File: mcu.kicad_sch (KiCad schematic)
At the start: 10 parts, among them J11 USB_C_Receptacle_USB2.0_16P, U4 ESP32-S3-WROOM-1, U5 STM32C011F4Ux

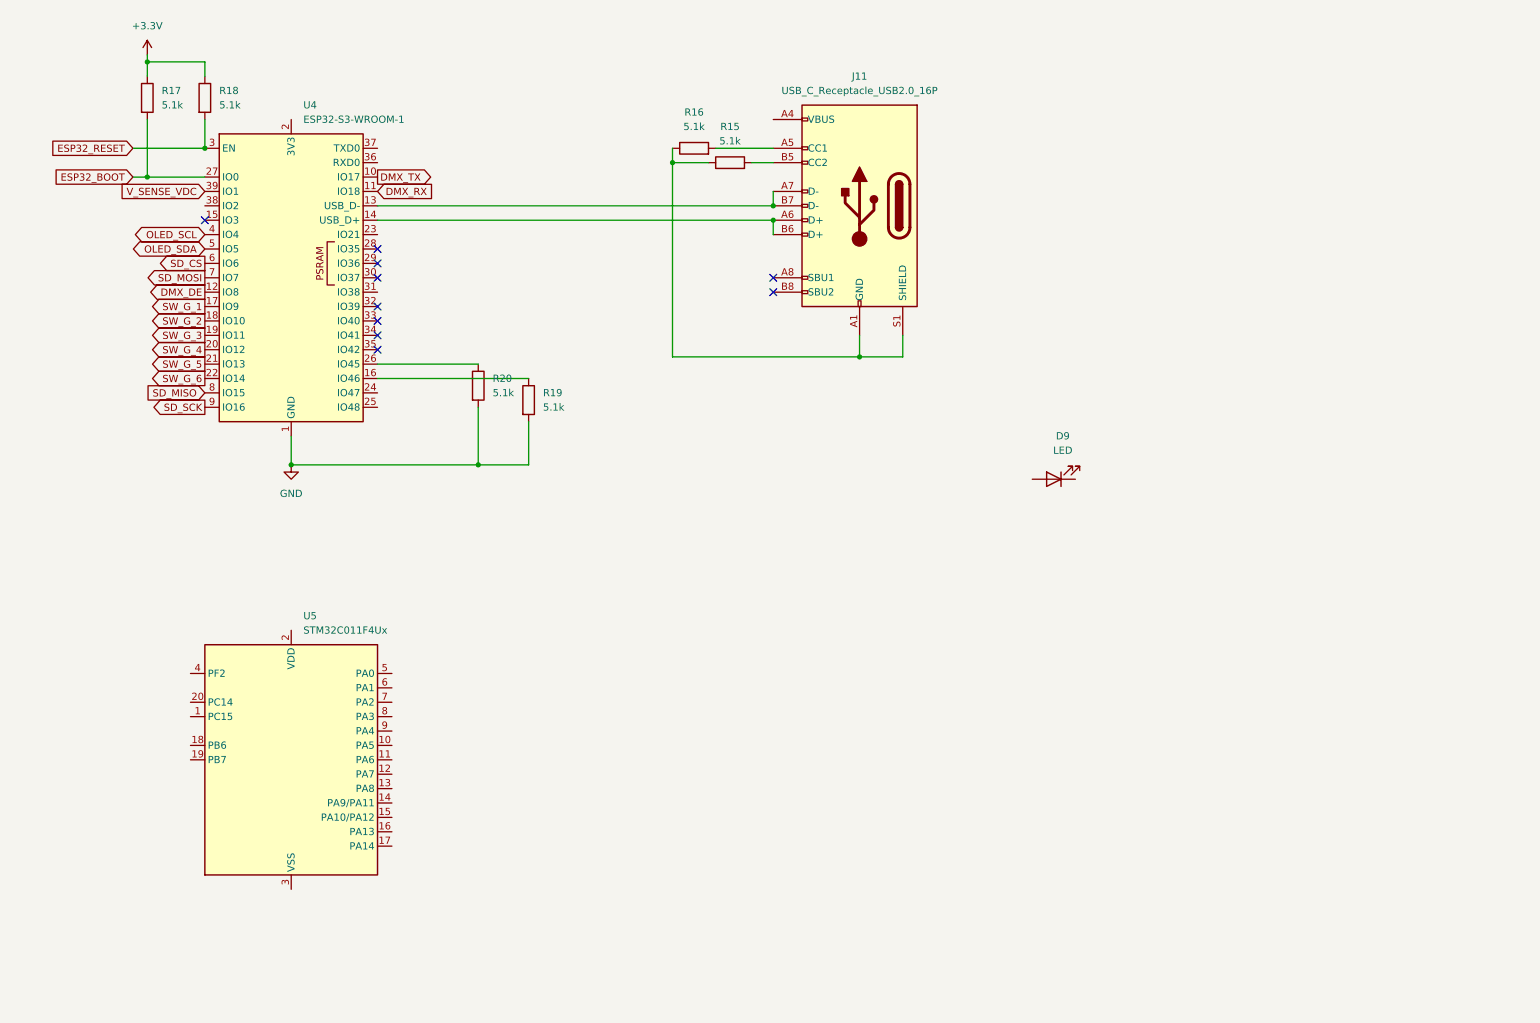
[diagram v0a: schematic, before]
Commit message: mcu pinouts and extras
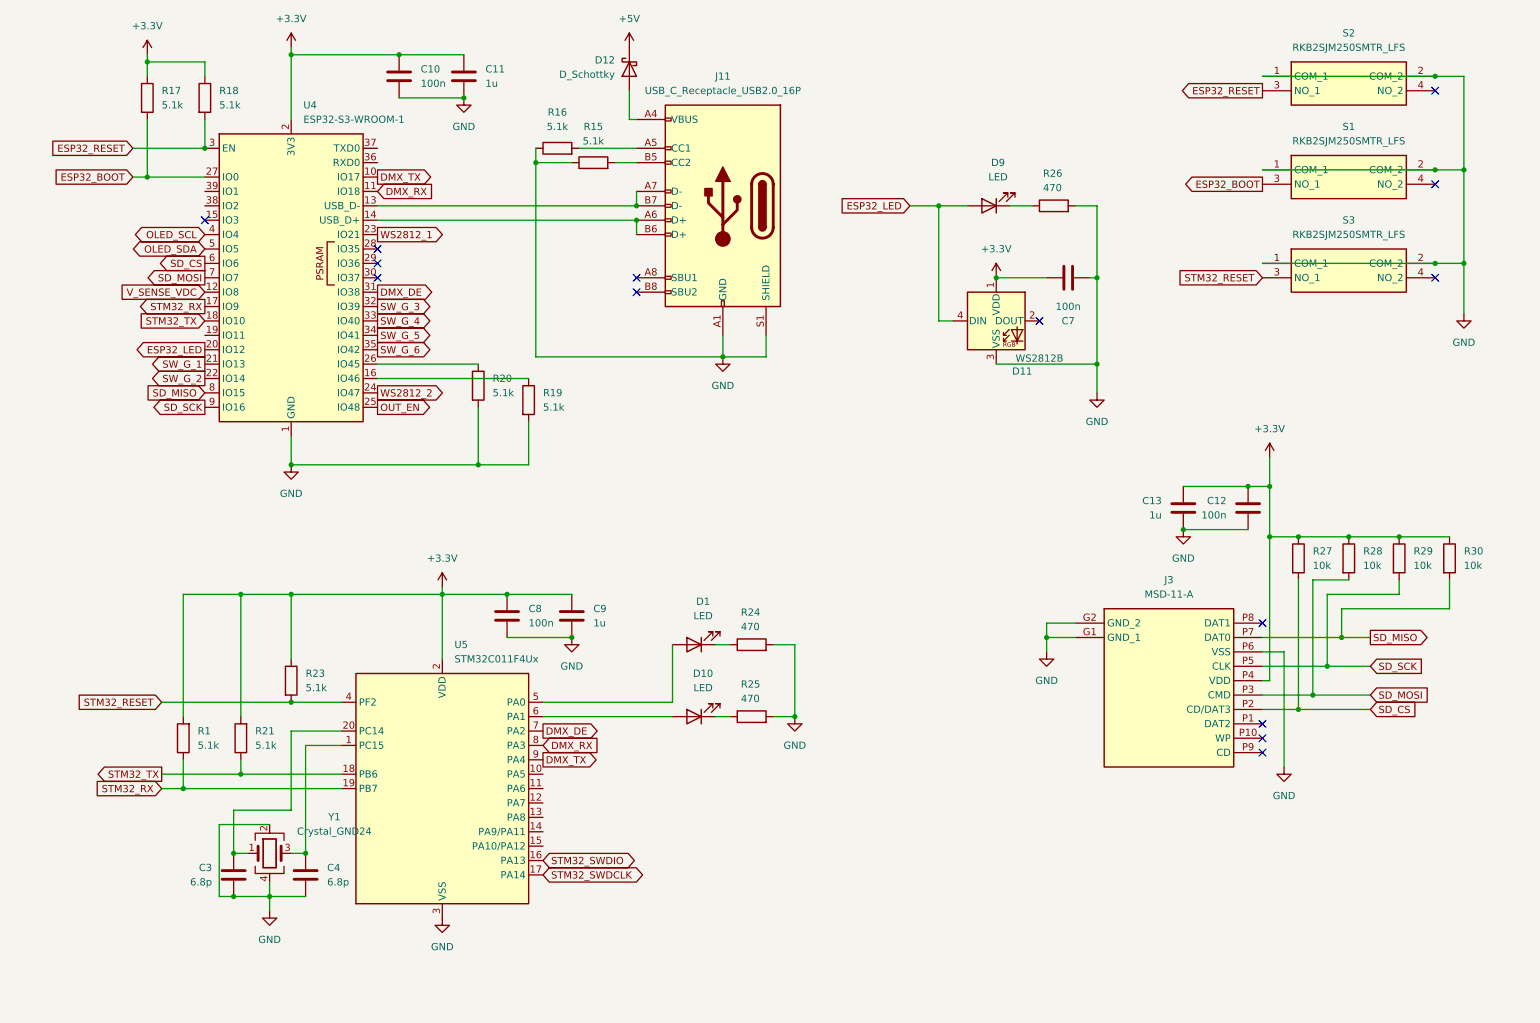
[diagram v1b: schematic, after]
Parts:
- added C10, C12, C7, C8: 100n, Capacitor_SMD:C_0603_1608Metric_Pad1.08x0.95mm_HandSolder, symbol Device:C
- added C11, C13, C9: 1u, Capacitor_SMD:C_0603_1608Metric_Pad1.08x0.95mm_HandSolder, symbol Device:C
- added C3, C4: 6.8p, Capacitor_SMD:C_0603_1608Metric_Pad1.08x0.95mm_HandSolder, symbol Device:C
- added D1, D10: LED, LED_SMD:LED_0603_1608Metric_Pad1.05x0.95mm_HandSolder, symbol Device:LED
- added D11: WS2812B, LED_SMD:LED_WS2812B_PLCC4_5.0x5.0mm_P3.2mm, symbol LED:WS2812B
- added D12: D_Schottky, Diode_SMD:D_SOD-323_HandSoldering, symbol Device:D_Schottky
- added J3: MSD-11-A, SamacSys_Parts:MSD11A, symbol SamacSys_Parts:MSD-11-A
- added R1, R21, R23: 5.1k, Resistor_SMD:R_0603_1608Metric_Pad0.98x0.95mm_HandSolder, symbol Device:R
- added R24, R25, R26: 470, Resistor_SMD:R_0603_1608Metric_Pad0.98x0.95mm_HandSolder, symbol Device:R
- added R27, R28, R29, R30: 10k, Resistor_SMD:R_0603_1608Metric_Pad0.98x0.95mm_HandSolder, symbol Device:R
- added S1, S2, S3: RKB2SJM250SMTR_LFS, SamacSys_Parts:RKB2SJM250SMTRLFS, symbol SamacSys_Parts:RKB2SJM250SMTR_LFS
- added Y1: Crystal_GND24, Crystal:Crystal_SMD_Abracon_ABM8AIG-4Pin_3.2x2.5mm, symbol Device:Crystal_GND24
- R17, R18, R19, R20: footprint (none) -> Resistor_SMD:R_0603_1608Metric_Pad0.98x0.95mm_HandSolder
- U4: footprint RF_Module:ESP32-S2-MINI-1 -> RF_Module:ESP32-S3-WROOM-2
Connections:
- net +3.3V: now also U4.2 (3V3), U5.2 (VDD), C10.1, C11.1, C12.1, C13.1, C7.1, C8.1, C9.1, D11.1 (VDD), J3.P4 (VDD), R1.2, R21.2, R23.1, R27.1, R28.1, R29.1, R30.1
- net DMX_DE: now also U4.31 (IO38), U5.7 (PA2); no longer U4.12 (IO8)
- net DMX_RX: now also U5.8 (PA3)
- net DMX_TX: now also U5.9 (PA4)
- net ESP32_BOOT: now also S1.3 (NO_1)
- net ESP32_RESET: now also S2.3 (NO_1)
- net GND: now also J11.A1 (GND), J11.A12 (GND), J11.B1 (GND), J11.B12 (GND), J11.S1 (SHIELD), R15.1, R16.1, U5.3 (VSS), C10.2, C11.2, C12.2, C13.2, C3.2, C4.2, C7.2, C8.2, C9.2, D11.3 (VSS), J3.G1 (GND_1), J3.G2 (GND_2), J3.P6 (VSS), R24.2, R25.2, R26.2, S1.1 (COM_1), S1.2 (COM_2), S2.1 (COM_1), S2.2 (COM_2), S3.1 (COM_1), S3.2 (COM_2), Y1.2, Y1.4
- net SD_CS: now also J3.P2 (CD/DAT3), R27.2
- net SD_MISO: now also J3.P7 (DAT0), R30.2
- net SD_MOSI: now also J3.P3 (CMD), R28.2
- net SD_SCK: now also J3.P5 (CLK), R29.2
- net SW_G_1: now also U4.21 (IO13); no longer U4.17 (IO9)
- net SW_G_2: now also U4.22 (IO14); no longer U4.18 (IO10)
- net SW_G_3: now also U4.32 (IO39); no longer U4.19 (IO11)
- net SW_G_4: now also U4.33 (IO40); no longer U4.20 (IO12)
- net SW_G_5: now also U4.34 (IO41); no longer U4.21 (IO13)
- net SW_G_6: now also U4.35 (IO42); no longer U4.22 (IO14)
- net V_SENSE_VDC: now also U4.12 (IO8); no longer U4.39 (IO1)
- net WS2812_1: now reaches U4.23 (IO21)
- net WS2812_2: now reaches U4.24 (IO47)
- net OUT_EN: now reaches U4.25 (IO48)
- net at D9.1 (K): now also R26.1
- net ESP32_LED: now reaches D9.2 (A)
- net ESP32_LED: now also U4.20 (IO12), D11.4 (DIN)
- net at U5.1 (PC15): now also C4.1, Y1.3
- net STM32_SWDIO: now reaches U5.16 (PA13)
- net STM32_SWDCLK: now reaches U5.17 (PA14)
- net STM32_TX: now reaches U5.18 (PB6)
- net STM32_TX: now also U4.18 (IO10), R21.1
- net STM32_RX: now reaches U5.19 (PB7)
- net STM32_RX: now also U4.17 (IO9), R1.1
- net at U5.20 (PC14): now also C3.1, Y1.1
- net STM32_RESET: now reaches U5.4 (PF2)
- net STM32_RESET: now also R23.2, S3.3 (NO_1)
- net at U5.5 (PA0): now also D1.2 (A)
- net at U5.6 (PA1): now also D10.2 (A)
- net at J11.A4 (VBUS), J11.A9 (VBUS), J11.B4 (VBUS)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: now also D12.2 (A)
- new net: D1.1 (K), R24.1
- new net: D10.1 (K), R25.1
- new net +5V: D12.1 (K)
- no-connect marks 10 -> 14
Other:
- moved on the sheet: D9, J11, R15, R16, U5

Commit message: power circuitry
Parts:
- removed D12: D_Schottky, Diode_SMD:D_SOD-323_HandSoldering, symbol Device:D_Schottky
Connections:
- net VBUS: now reaches J11.A4 (VBUS), J11.A9 (VBUS), J11.B4 (VBUS), J11.B9 (VBUS)
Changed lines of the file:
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@@
 	(wire
 		(pts
-			(xy 125.73 33.02) (xy 125.73 38.1)
+			(xy 125.73 30.48) (xy 125.73 38.1)
 		)
 		(stroke
@@
 	)
 	(global_label "STM32_RESET"
-		(shape input)
+		(shape output)
 		(at 237.49 66.04 180)
 		(fields_autoplaced yes)
@@
 	)
 	(symbol
-		(lib_id "Device:D_Schottky")
-		(at 125.73 29.21 90)
-		(mirror x)
-		(unit 1)
-		(exclude_from_sim no)
-		(in_bom yes)
-		(on_board yes)
-		(dnp no)
-		(property "Reference" "D12"
-			(at 123.19 27.6224 90)
-			(effects
-				(font
-					(size 1.27 1.27)
-				)
-				(justify left)
-			)
-		)
-		(property "Value" "D_Schottky"
-			(at 123.19 30.1624 90)
-			(effects
-				(font
-					(size 1.27 1.27)
-				)
-				(justify left)
-			)
-		)
-		(property "Footprint" "Diode_SMD:D_SOD-323_HandSoldering"
-			(at 125.73 29.21 0)
-			(effects
-				(font
-					(size 1.27 1.27)
-				)
-				(hide yes)
-			)
-		)
-		(property "Datasheet" "~"
-			(at 125.73 29.21 0)
-			(effects
-				(font
-					(size 1.27 1.27)
-				)
-				(hide yes)
-			)
-		)
-		(property "Description" "Schottky diode"
-			(at 125.73 29.21 0)
-			(effects
-				(font
-					(size 1.27 1.27)
-				)
-				(hide yes)
-			)
-		)
-		(pin "1"
-		)
-		(pin "2"
-		)
-		(instances
-			(project ""
-				(path "/bd7590c0-6a37-4bf0-a9f2-f26180744ceb/57a6da49-ac9c-48a2-9772-b91851c32cdb"
-					(reference "D12")
-					(unit 1)
-				)
-			)
-		)
-	)
-	(symbol
 		(lib_id "power:GND")
 		(at 96.52 34.29 0)
@@
 	)
 	(symbol
-		(lib_id "power:+5V")
-		(at 125.73 25.4 0)
-		(unit 1)
-		(exclude_from_sim no)
-		(in_bom yes)
-		(on_board yes)
-		(dnp no)
-		(fields_autoplaced yes)
-		(property "Reference" "#PWR025"
-			(at 125.73 29.21 0)
-			(effects
-				(font
-					(size 1.27 1.27)
-				)
-				(hide yes)
-			)
-		)
-		(property "Value" "+5V"
-			(at 125.73 20.32 0)
-			(effects
-				(font
-					(size 1.27 1.27)
-				)
-			)
-		)
-		(property "Footprint" ""
-			(at 125.73 25.4 0)
-			(effects
-				(font
-					(size 1.27 1.27)
-				)
-				(hide yes)
-			)
-		)
-		(property "Datasheet" ""
-			(at 125.73 25.4 0)
-			(effects
-				(font
-					(size 1.27 1.27)
-				)
-				(hide yes)
-			)
-		)
-		(property "Description" "Power symbol creates a global label with name \"+5V\""
-			(at 125.73 25.4 0)
-			(effects
-				(font
-					(size 1.27 1.27)
-				)
-				(hide yes)
-			)
-		)
-		(pin "1"
-		)
-		(instances
-			(project ""
-				(path "/bd7590c0-6a37-4bf0-a9f2-f26180744ceb/57a6da49-ac9c-48a2-9772-b91851c32cdb"
-					(reference "#PWR025")
-					(unit 1)
-				)
-			)
-		)
-	)
-	(symbol
 		(lib_id "Device:C")
 		(at 68.58 171.45 0)
@@
 					(unit 1)
 				)
+			)
+		)
+	)
+	(symbol
+		(lib_id "power:VBUS")
+		(at 125.73 30.48 0)
+		(unit 1)
+		(exclude_from_sim no)
+		(in_bom yes)
+		(on_board yes)
+		(dnp no)
+		(fields_autoplaced yes)
+		(property "Reference" "#PWR025"
+			(at 125.73 34.29 0)
+			(effects
+				(font
+					(size 1.27 1.27)
+				)
+				(hide yes)
+			)
+		)
+		(property "Value" "VBUS"
+			(at 125.73 25.4 0)
+			(effects
+				(font
+					(size 1.27 1.27)
+				)
+			)
+		)
+		(property "Footprint" ""
+			(at 125.73 30.48 0)
+			(effects
+				(font
+					(size 1.27 1.27)
+				)
+				(hide yes)
+			)
+		)
+		(property "Datasheet" ""
+			(at 125.73 30.48 0)
+			(effects
+				(font
+					(size 1.27 1.27)
+				)
+				(hide yes)
+			)
+		)
+		(property "Description" "Power symbol creates a global label with name \"VBUS\""
+			(at 125.73 30.48 0)
+			(effects
+				(font
+					(size 1.27 1.27)
+				)
+				(hide yes)
+			)
+		)
+		(pin "1"
+		)
+		(instances
+			(project ""
+				(path "/bd7590c0-6a37-4bf0-a9f2-f26180744ceb/57a6da49-ac9c-48a2-9772-b91851c32cdb"
+					(reference "#PWR025")
+					(unit 1)
+				)

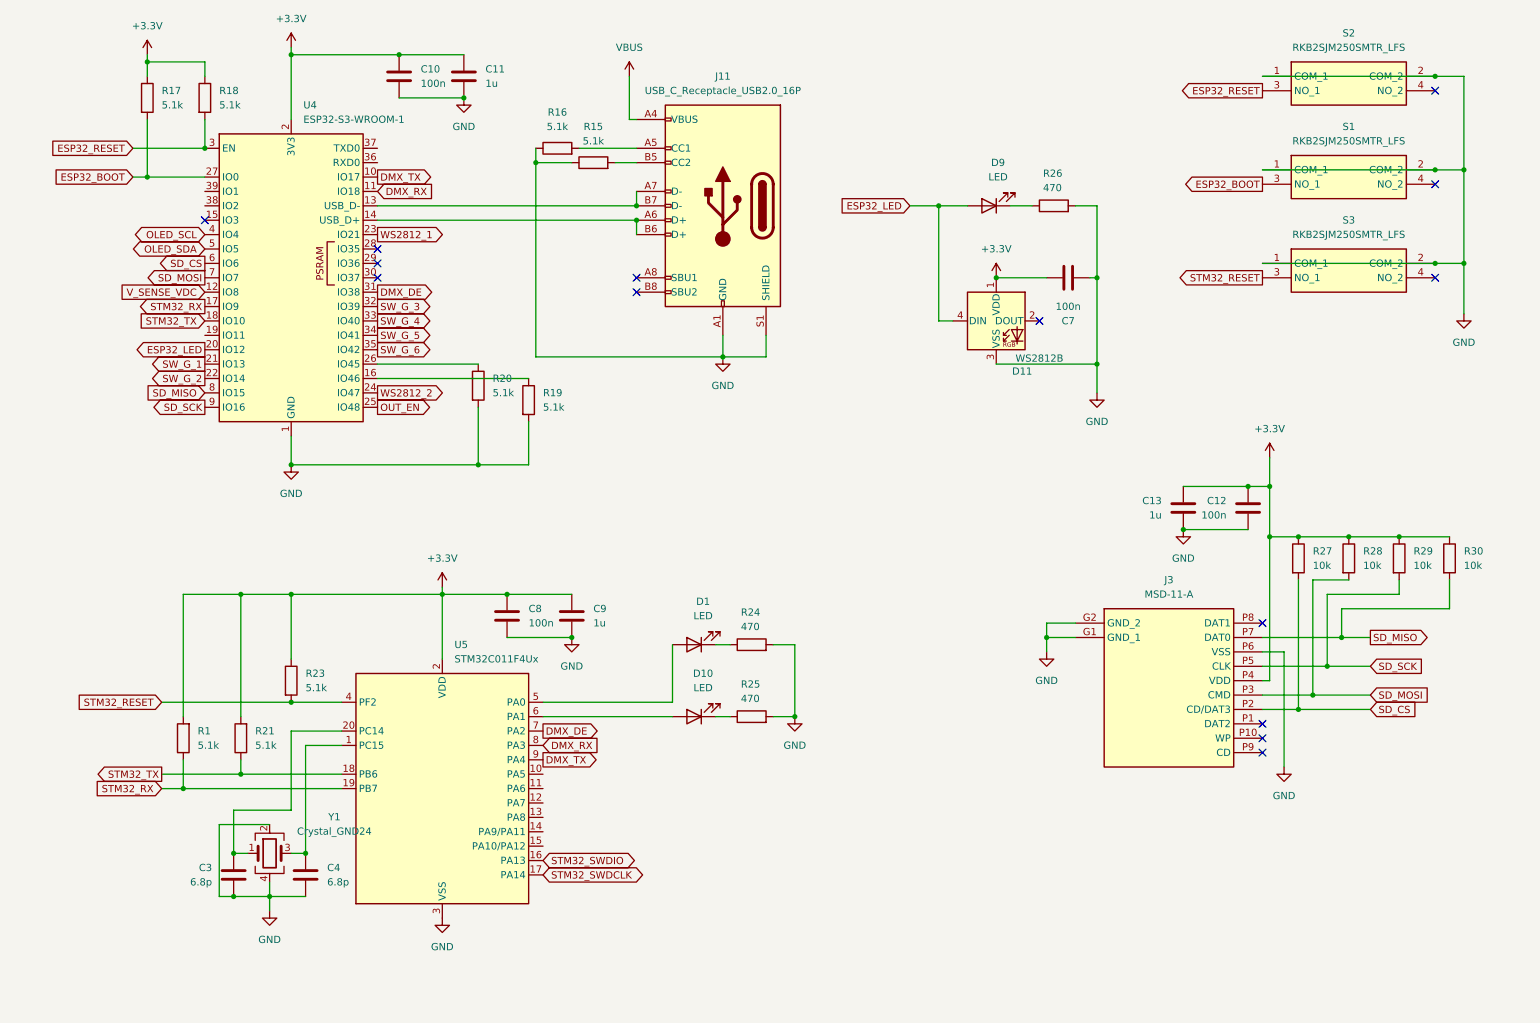
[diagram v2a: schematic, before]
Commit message: add probe headers
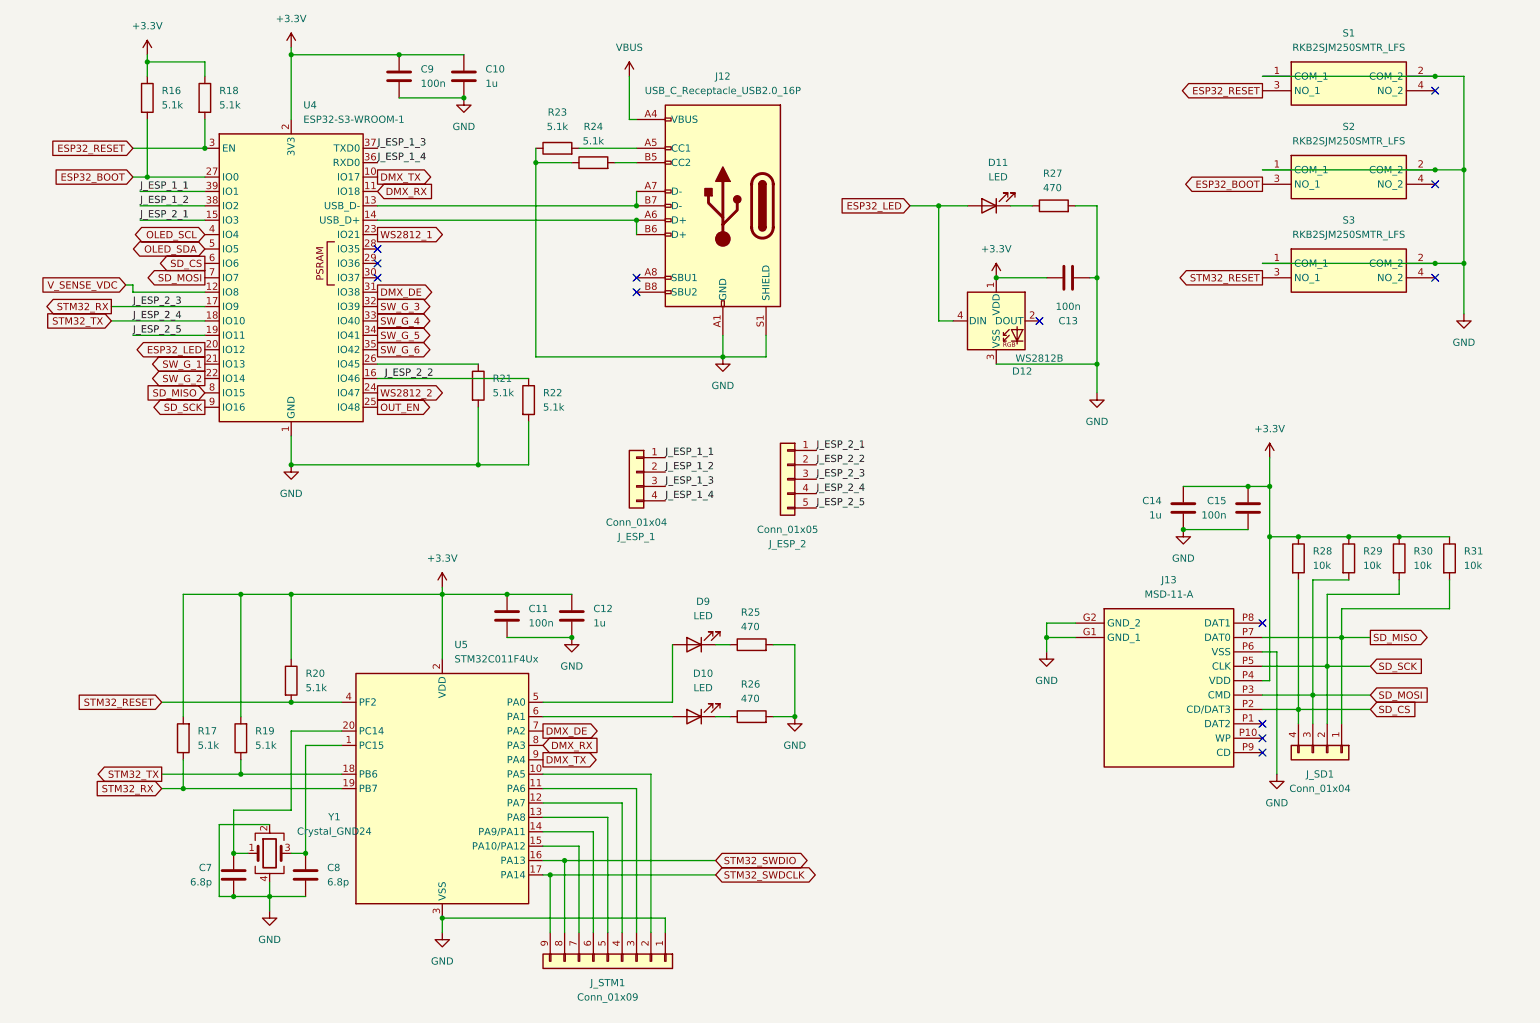
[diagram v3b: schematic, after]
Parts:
- added J_ESP_1, J_SD1: Conn_01x04, Connector_PinHeader_2.54mm:PinHeader_1x04_P2.54mm_Vertical, symbol Connector_Generic:Conn_01x04
- added J_ESP_2: Conn_01x05, Connector_PinSocket_2.54mm:PinSocket_1x05_P2.54mm_Vertical, symbol Connector_Generic:Conn_01x05
- added J_STM1: Conn_01x09, Connector_PinHeader_2.54mm:PinHeader_1x09_P2.54mm_Vertical, symbol Connector_Generic:Conn_01x09
- renumbered C11 to C10, C8 to C11, C9 to C12, C7 to C13, C13 to C14, C12 to C15, C3 to C7, C4 to C8, C10 to C9, D9 to D11, D11 to D12, D1 to D9, J11 to J12, J3 to J13, R17 to R16, R1 to R17, R21 to R19, R23 to R20, R20 to R21, R19 to R22, R16 to R23, R15 to R24, R24 to R25, R25 to R26, R26 to R27, R27 to R28, R28 to R29, R29 to R30, R30 to R31, S2 to S1, S1 to S2
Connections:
- net GND: now also J_STM1.1 (Pin_1)
- net SD_CS: now also J_SD1.4 (Pin_4)
- net SD_MISO: now also J_SD1.1 (Pin_1)
- net SD_MOSI: now also J_SD1.3 (Pin_3)
- net SD_SCK: now also J_SD1.2 (Pin_2)
- net STM32_RX: now also J_ESP_2.3 (Pin_3)
- net STM32_SWDCLK: now also J_STM1.9 (Pin_9)
- net STM32_SWDIO: now also J_STM1.8 (Pin_8)
- net STM32_TX: now also J_ESP_2.4 (Pin_4)
- net J_ESP_2_1: now reaches U4.15 (IO3)
- net J_ESP_2_1: now also J_ESP_2.1 (Pin_1)
- net J_ESP_2_2: now reaches R22.1, U4.16 (IO46)
- net J_ESP_2_2: now also J_ESP_2.2 (Pin_2)
- net J_ESP_2_5: now reaches U4.19 (IO11)
- net J_ESP_2_5: now also J_ESP_2.5 (Pin_5)
- net J_ESP_1_4: now reaches U4.36 (RXD0)
- net J_ESP_1_4: now also J_ESP_1.4 (Pin_4)
- net J_ESP_1_3: now reaches U4.37 (TXD0)
- net J_ESP_1_3: now also J_ESP_1.3 (Pin_3)
- net J_ESP_1_2: now reaches U4.38 (IO2)
- net J_ESP_1_2: now also J_ESP_1.2 (Pin_2)
- net J_ESP_1_1: now reaches U4.39 (IO1)
- net J_ESP_1_1: now also J_ESP_1.1 (Pin_1)
- net at U5.10 (PA5): now also J_STM1.2 (Pin_2)
- net at U5.11 (PA6): now also J_STM1.3 (Pin_3)
- net at U5.12 (PA7): now also J_STM1.4 (Pin_4)
- net at U5.13 (PA8): now also J_STM1.5 (Pin_5)
- net at U5.14 (PA9/PA11): now also J_STM1.6 (Pin_6)
- net at U5.15 (PA10/PA12): now also J_STM1.7 (Pin_7)
- no-connect marks 14 -> 13

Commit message: partial layout
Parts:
- added J_OLED_1: Conn_01x04, Connector_PinHeader_2.54mm:PinHeader_1x04_P2.54mm_Vertical, symbol Connector_Generic:Conn_01x04
- renumbered C8 to C10, C9 to C11, C10 to C12, C11 to C13, C12 to C14, C13 to C15, C14 to C16, C15 to C17, C7 to C9, R16 to R17, R17 to R18, R18 to R19, R19 to R20, R20 to R21, R21 to R22, R22 to R23, R23 to R24, R24 to R25, R25 to R26, R26 to R27, R27 to R28, R28 to R29, R29 to R30, R30 to R31, R31 to R32
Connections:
- net +3.3V: now also J_OLED_1.1 (Pin_1)
- net GND: now also J_OLED_1.2 (Pin_2)
- net OLED_SCL: now also J_OLED_1.3 (Pin_3)
- net OLED_SDA: now also J_OLED_1.4 (Pin_4)
- net USB-: now reaches J12.A7 (D-), J12.B7 (D-), U4.13 (USB_D-)
- net USB+: now reaches J12.A6 (D+), J12.B6 (D+), U4.14 (USB_D+)
